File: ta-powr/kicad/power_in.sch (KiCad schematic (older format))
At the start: 29 parts, among them U1 SPV1040, U3 TLV8544DT, U4 ADS1115-Q1

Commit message: first crack at parts placement on power board
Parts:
- removed C18: DNP, ta-powr:TECATE_PBL, symbol Device:CP1
- gave numbers to parts that had none: 1
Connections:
- net V_cap is gone; now on net Vcap: C6.1, C7.1, R2.1, R20.1, R27.1
- net V_harv: now also L1.1, R1.2; no longer C3.1, R1.1, U1.1 (MPP-SET), U1.8 (XSHUT)
- net Vdd_IN_loc renamed Vdd_loc
- new net: C3.1, R1.1, U1.1 (MPP-SET), U1.8 (XSHUT)
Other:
- moved on the sheet: C1, C2, L1, R1, R19, R21, R22, R23, R24, R25, R26, R27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

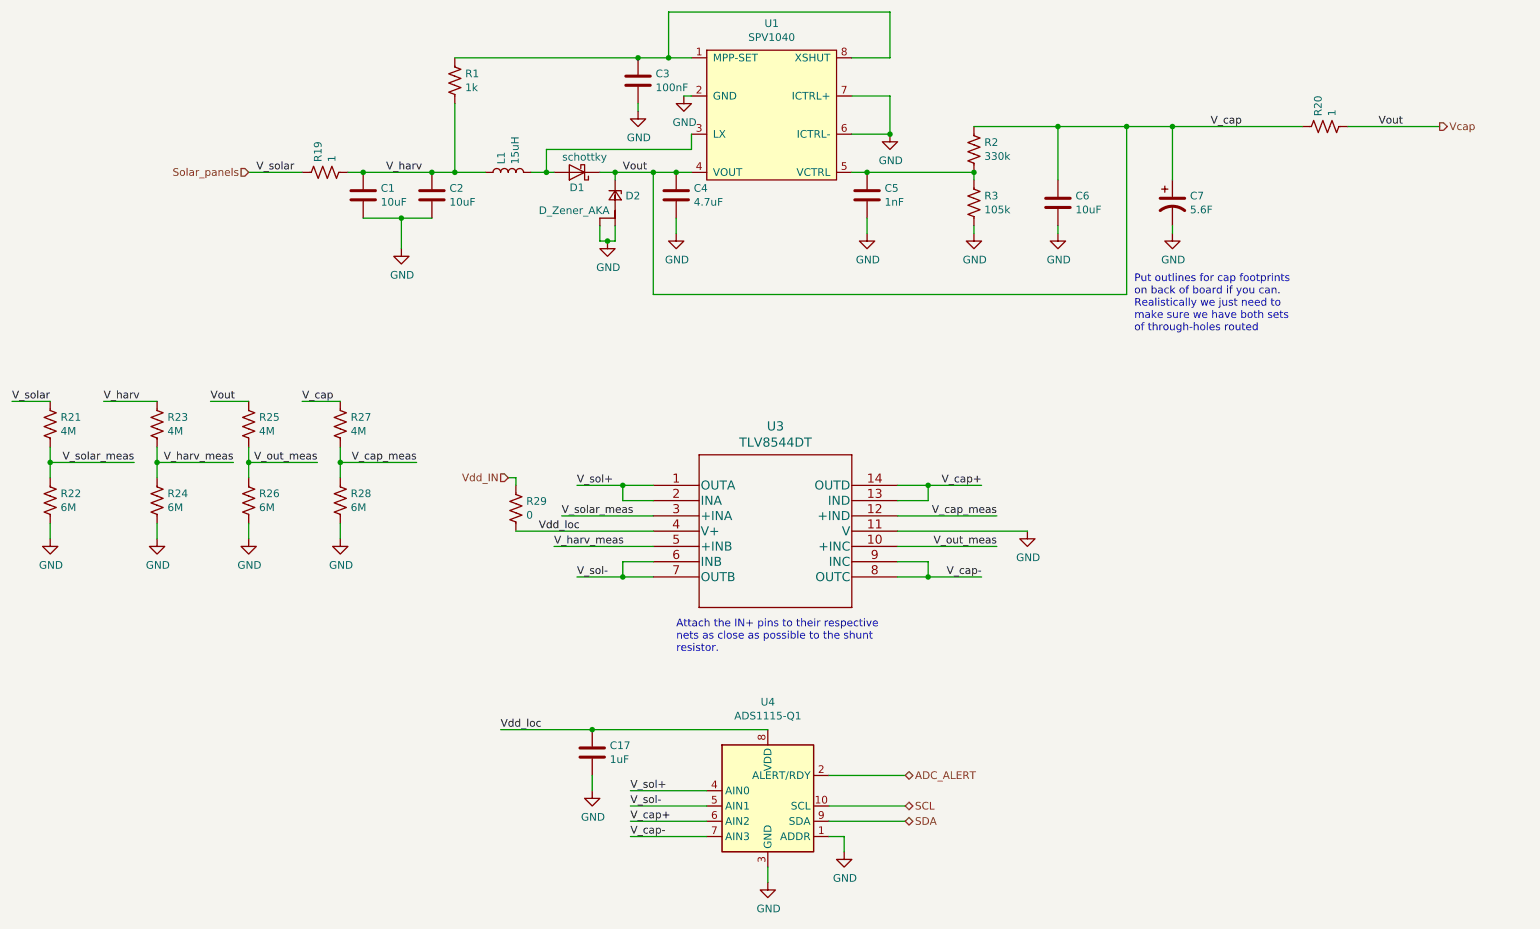
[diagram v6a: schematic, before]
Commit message: layout redone after pinout changes
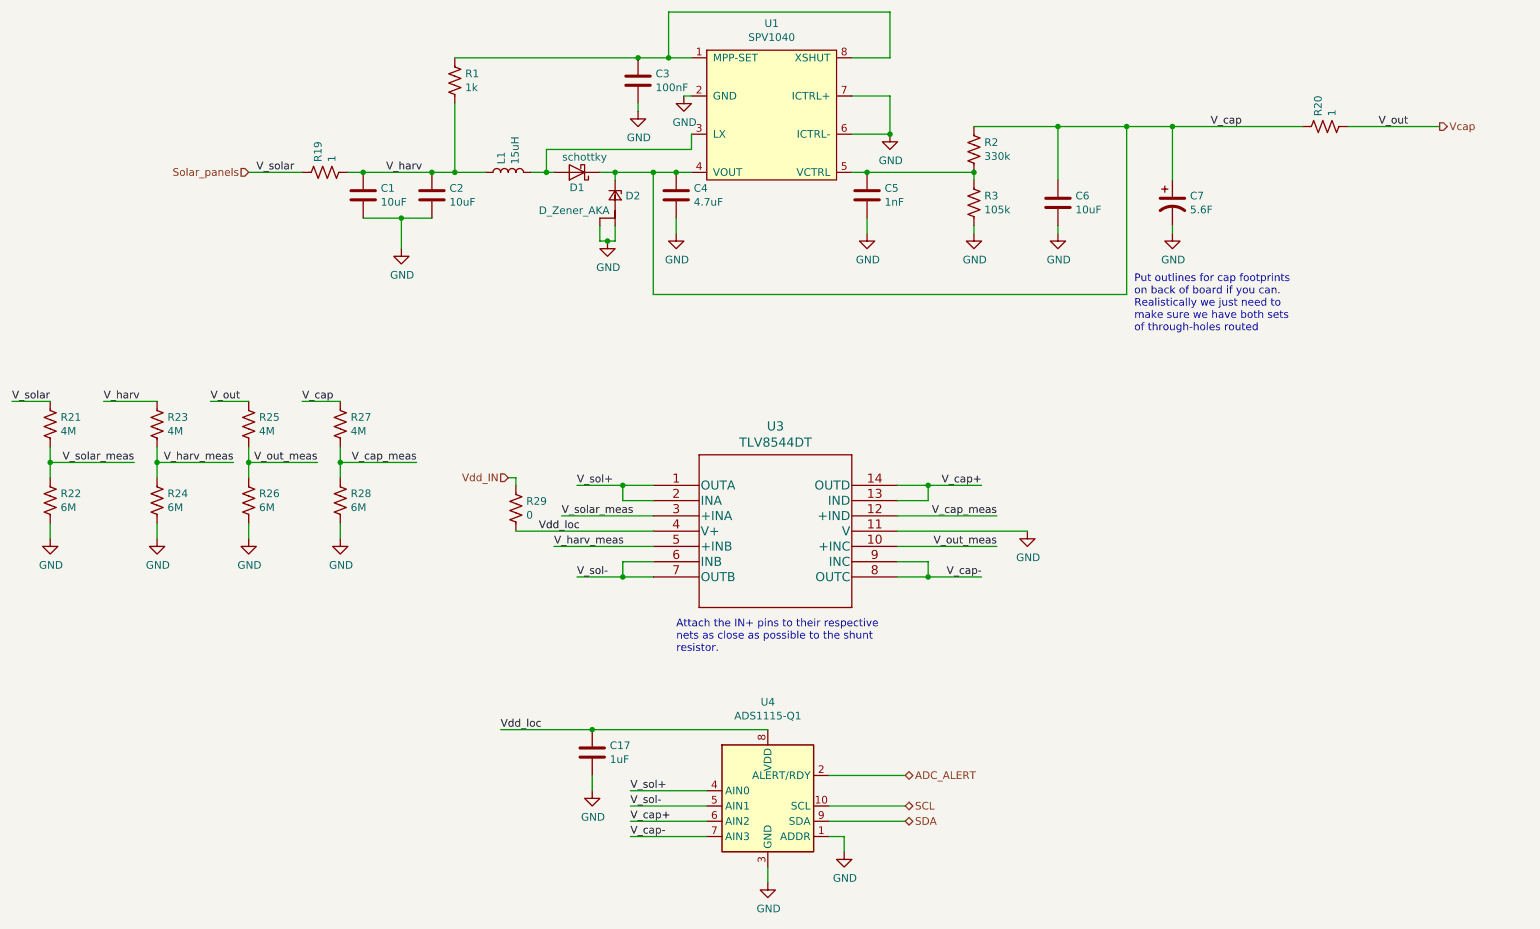
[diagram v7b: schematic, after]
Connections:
- net Vcap: no longer C4.1, C6.1, C7.1, D1.1 (K), D2.2 (K), R2.1, R20.1, R27.1, U1.4 (VOUT)
- new net V_cap: C4.1, C6.1, C7.1, D1.1 (K), D2.2 (K), R2.1, R20.1, R27.1, U1.4 (VOUT)
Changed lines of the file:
@@
 Wire Wire Line
 	4900 2600 4900 2700
-Text Label 4550 2300 0    50   ~ 0
-Vout
 $Comp
 L Device:C C5
@@
 	8150 2650 8150 2700
 Text Label 9500 2000 0    50   ~ 0
-Vout
+V_out
 Connection ~ 8150 2000
 Text Notes 7900 3350 0    50   ~ 0
@@
 V_cap
 Text Label 1850 3800 0    50   ~ 0
-Vout
+V_out
 Text Notes 4900 5450 0    50   ~ 0
 Attach the IN+ pins to their respective\nnets as close as possible to the shunt\nresistor.

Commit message: Added all wires except for GND connections
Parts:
- added R30: 0, Resistor_SMD:R_0603_1608Metric, symbol Device:R_US
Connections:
- net V_cap+: now also U4.7 (AIN3); no longer U4.6 (AIN2)
- net V_cap-: now also U4.6 (AIN2); no longer U4.7 (AIN3)
- net Vdd_IN: now also R30.2
- net Vdd_loc renamed Vdd_adc
- net Vdd_adc: now also R30.1; no longer R29.2, U3.4 (V+)
- new net Vdd_tlv: R29.2, U3.4 (V+)
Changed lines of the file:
@@
 	1    0    0    -1
 $EndComp
-Text HLabel 3800 4300 0    50   Input ~ 0
+Text HLabel 3600 4300 0    50   Input ~ 0
 Vdd_IN
 Wire Wire Line
@@
 Wire Wire Line
 	5100 6650 4600 6650
+Text Label 4600 6650 0    50   ~ 0
+V_cap+
 Text Label 4600 6550 0    50   ~ 0
-V_cap+
-Text Label 4600 6650 0    50   ~ 0
 V_cap-
 Connection ~ 6550 4950
@@
 Wire Wire Line
 	3750 5950 4350 5950
-Text Label 3750 5950 0    50   ~ 0
-Vdd_loc
 Wire Wire Line
 	4250 4350 4550 4350
@@
 	1500 4100 1500 4200
 Text Label 4000 4650 0    50   ~ 0
-Vdd_loc
+Vdd_tlv
 Connection ~ 2700 4200
 Wire Wire Line
@@
 Wire Wire Line
 	2700 4600 2700 4700
-$Comp
-L Device:R_US R29
-U 1 1 5F183712
-P 3850 4500
-F 0 "R29" H 3918 4546 50  0000 L CNN
-F 1 "0" H 3918 4455 50  0000 L CNN
-F 2 "Resistor_SMD:R_0603_1608Metric" V 3890 4490 50  0001 C CNN
-F 3 "~" H 3850 4500 50  0001 C CNN
-	1    3850 4500
-	1    0    0    -1
-$EndComp
-Wire Wire Line
-	3800 4300 3850 4300
 Wire Wire Line
 	3850 4300 3850 4350
@@
 	0    -1   -1   0
 $EndComp
+$Comp
+L Device:R_US R29
+U 1 1 5F183712
+P 3850 4500
+F 0 "R29" H 3918 4546 50  0000 L CNN
+F 1 "0" H 3918 4455 50  0000 L CNN
+F 2 "Resistor_SMD:R_0603_1608Metric" V 3890 4490 50  0001 C CNN
+F 3 "~" H 3850 4500 50  0001 C CNN
+	1    3850 4500
+	1    0    0    -1
+$EndComp
+$Comp
+L Device:R_US R30
+U 1 1 5F12BE3B
+P 3750 5550
+F 0 "R30" H 3818 5596 50  0000 L CNN
+F 1 "0" H 3818 5505 50  0000 L CNN
+F 2 "Resistor_SMD:R_0603_1608Metric" V 3790 5540 50  0001 C CNN
+F 3 "~" H 3750 5550 50  0001 C CNN
+	1    3750 5550
+	1    0    0    1
+$EndComp
+Wire Wire Line
+	3600 4300 3750 4300
+Wire Wire Line
+	3750 4300 3750 5400
+Connection ~ 3750 4300
+Wire Wire Line
+	3750 4300 3850 4300
+Wire Wire Line
+	3750 5700 3750 5950
+Text Label 3850 5950 0    50   ~ 0
+Vdd_adc
 $EndSCHEMATC
